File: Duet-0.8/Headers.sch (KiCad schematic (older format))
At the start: 20 parts, among them J1 EXPANSION, J10 E0 MOT/STOP, J11 BED-, J12 V+, J13 GND, J14 BED POWER, J2 CONN2, J20 POWER IN, J23 Z MOT 2, J24 GND V_IN, J25 PS 5V, J28 Probe, J4 V+, J5 BED TEMP, J6 CONN2, J7 Z MOT/STOP, J8 Y MOT/STOP, J9 X MOT/STOP, P1 CONN_4

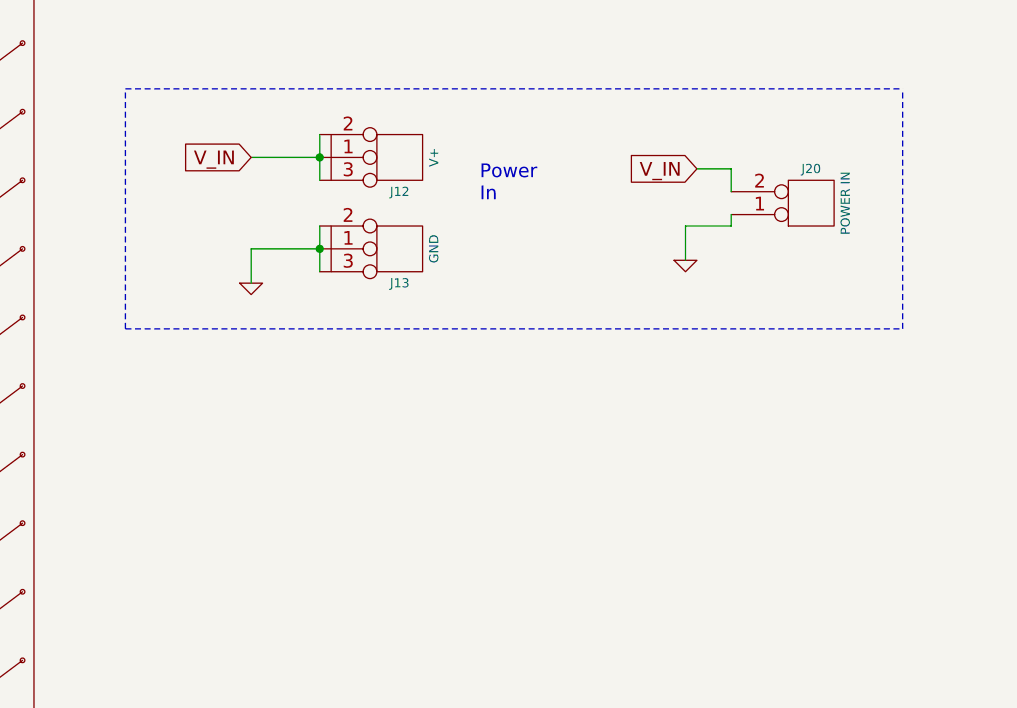
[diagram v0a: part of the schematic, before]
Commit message: USB B connector used.  Always-on fan connector added next to heater connector. Green power LED (5v) now has a bigger ballast resistor.
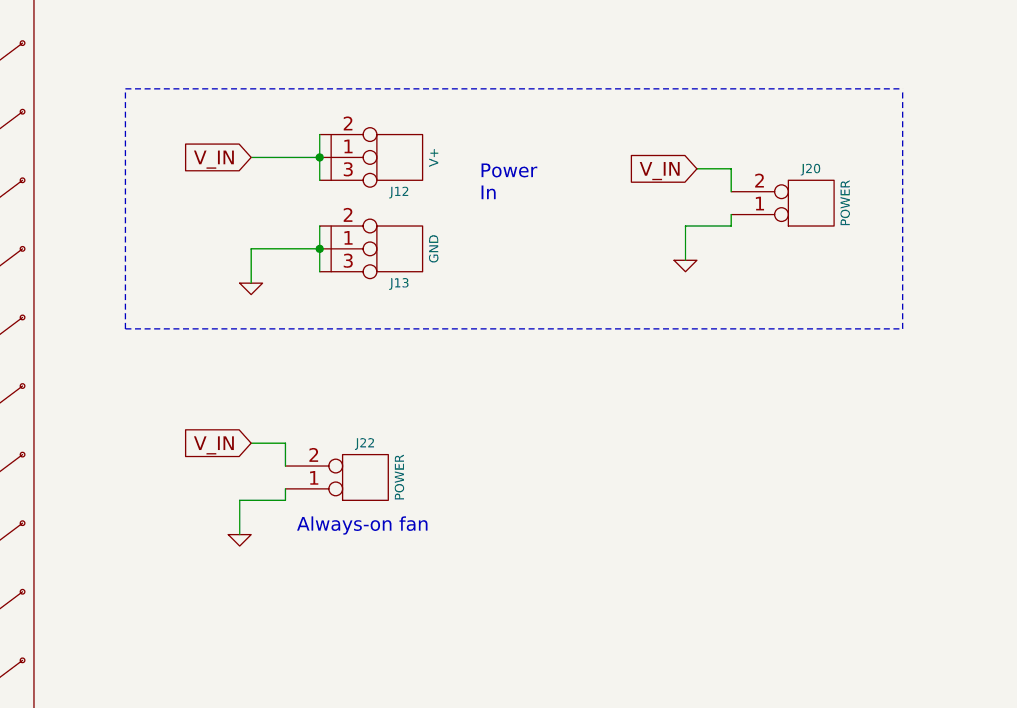
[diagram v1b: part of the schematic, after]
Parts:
- added J22: POWER, symbol CONN2
- J20: value POWER IN -> POWER
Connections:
- net GND: now also J22.1 (P1)
- net V_IN: now also J22.2 (PM)
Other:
- note added: "Always-on fan"
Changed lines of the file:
@@
 Sheet 4 7
 Title "Duet"
-Date "18 mar 2015"
+Date "8 jul 2015"
 Rev "0.7"
 Comp "Think3DPrint3D, RepRapPro"
@@
 P 5800 4950
 F 0 "J20" H 5800 4850 40  0000 C CNN
-F 1 "POWER IN" V 5950 5000 40  0000 C CNN
+F 1 "POWER" V 5950 5000 40  0000 C CNN
 F 2 "" H 5800 4950 60  0001 C CNN
 F 3 "" H 5800 4950 60  0001 C CNN
@@
 Wire Wire Line
 	6250 2150 6150 2150
+$Comp
+L CONN2 J22
+U 1 1 559D50DB
+P 3850 6150
+F 0 "J22" H 3850 6050 40  0000 C CNN
+F 1 "POWER" V 4000 6200 40  0000 C CNN
+F 2 "" H 3850 6150 60  0001 C CNN
+F 3 "" H 3850 6150 60  0001 C CNN
+	1    3850 6150
+	1    0    0    1
+$EndComp
+Text GLabel 3350 6050 0    60   Input ~ 0
+V_IN
+$Comp
+L GND #PWR040
+U 1 1 559D50E2
+P 3300 6450
+F 0 "#PWR040" H 3300 6450 30  0001 C CNN
+F 1 "GND" H 3300 6380 30  0001 C CNN
+F 2 "" H 3300 6450 60  0001 C CNN
+F 3 "" H 3300 6450 60  0001 C CNN
+	1    3300 6450
+	1    0    0    -1
+$EndComp
+Wire Wire Line
+	3300 6450 3300 6300
+Wire Wire Line
+	3350 6050 3500 6050
+Wire Wire Line
+	3500 6050 3500 6150
+Wire Wire Line
+	3500 6250 3500 6300
+Wire Wire Line
+	3500 6300 3300 6300
+Text Notes 3550 6450 0    60   ~ 0
+Always-on fan
 $EndSCHEMATC

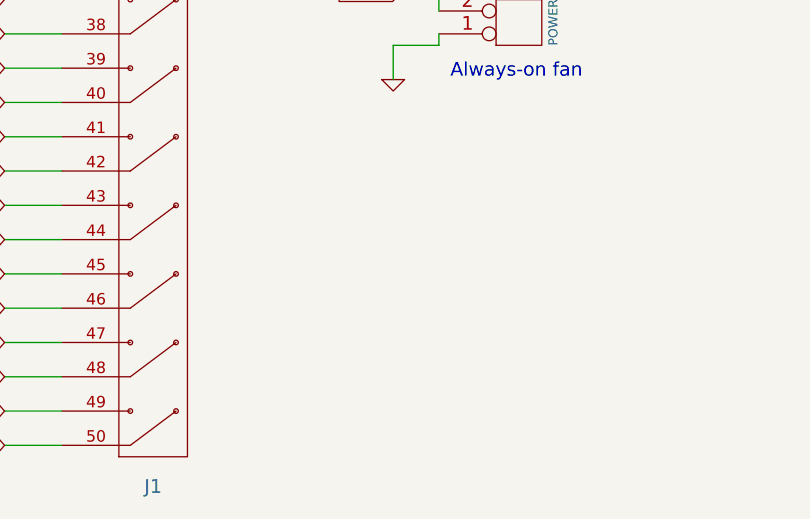
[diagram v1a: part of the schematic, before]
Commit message: Erase and Reset buttons replaced by jumpers.
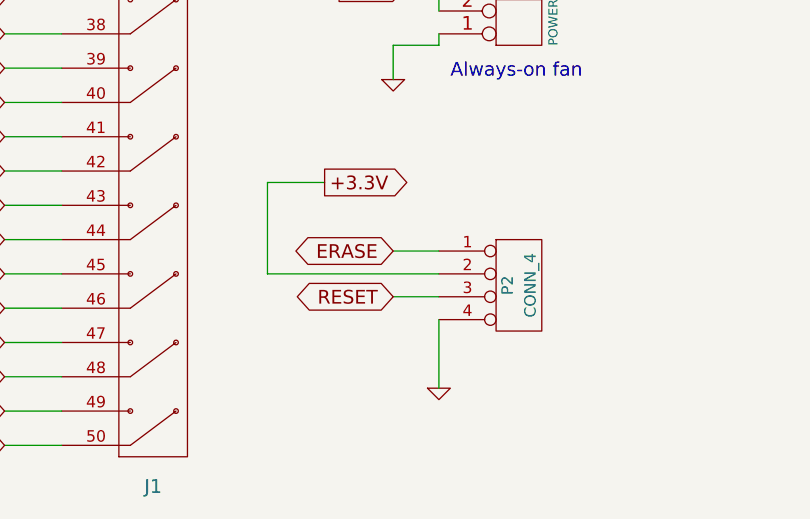
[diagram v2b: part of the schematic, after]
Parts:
- added P2: CONN_4, symbol CONN_4
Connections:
- net +3.3V: now also P2.2 (P2)
- net GND: now also P2.4 (P4)
- net RESET: now also P2.3 (P3)
- new net ERASE: P2.1 (P1)
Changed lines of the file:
@@
 Text Notes 3550 6450 0    60   ~ 0
 Always-on fan
+$Comp
+L CONN_4 P2
+U 1 1 559D9C48
+P 3850 7350
+F 0 "P2" V 3800 7350 50  0000 C CNN
+F 1 "CONN_4" V 3900 7350 50  0000 C CNN
+F 2 "" H 3850 7350 60  0000 C CNN
+F 3 "" H 3850 7350 60  0000 C CNN
+	1    3850 7350
+	1    0    0    -1
+$EndComp
+Text GLabel 3300 7200 0    60   BiDi ~ 0
+ERASE
+Wire Wire Line
+	3500 7200 3300 7200
+Text GLabel 3300 7400 0    60   BiDi ~ 0
+RESET
+Wire Wire Line
+	3500 7400 3300 7400
+Wire Wire Line
+	3500 7300 2750 7300
+$Comp
+L GND #PWR041
+U 1 1 559DA387
+P 3500 7800
+F 0 "#PWR041" H 3500 7800 30  0001 C CNN
+F 1 "GND" H 3500 7730 30  0001 C CNN
+F 2 "" H 3500 7800 60  0001 C CNN
+F 3 "" H 3500 7800 60  0001 C CNN
+	1    3500 7800
+	1    0    0    -1
+$EndComp
+Wire Wire Line
+	3500 7500 3500 7800
+Text GLabel 3000 6900 2    60   Output ~ 0
++3.3V
+Wire Wire Line
+	3000 6900 2750 6900
+Wire Wire Line
+	2750 6900 2750 7300
 $EndSCHEMATC

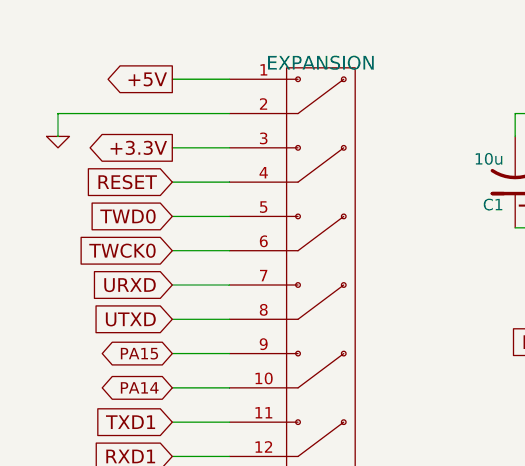
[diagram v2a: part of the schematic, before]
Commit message: Reset pin on the expansion header changed to V_IN now we have a reset pin on the board.  There was no V_IN on that header before, and it would be useful.
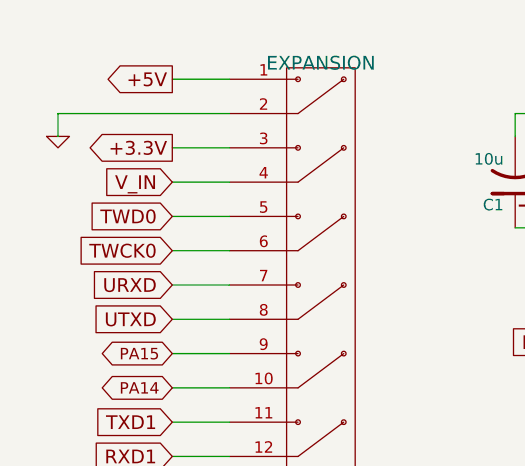
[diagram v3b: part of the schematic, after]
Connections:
- net RESET: no longer J1.4
- net V_IN: now also J1.4
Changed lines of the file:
@@
 Sheet 4 7
 Title "Duet"
-Date "8 jul 2015"
+Date "9 jul 2015"
 Rev "0.7"
 Comp "Think3DPrint3D, RepRapPro"
@@
 Text GLabel 1600 1750 0    60   Input ~ 0
 UTXD
-Text GLabel 1600 1150 0    60   Input ~ 0
-RESET
 Text GLabel 8250 6000 0    60   Input ~ 0
 VSSA
@@
 Wire Wire Line
 	2750 6900 2750 7300
+Text GLabel 1600 1150 0    60   Input ~ 0
+V_IN
 $EndSCHEMATC
